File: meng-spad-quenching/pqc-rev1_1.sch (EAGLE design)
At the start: 54 parts, among them IC1 ADCMP582, IC3 LT3032-5, J1 VIN_LOGIC, U1 SN65EPT21DGK, U2 TPS78233DDCT, U3 SN65EPT22DGK, X1 CONN_SPAD, X2 CONN_SCOPE_COMP, X3 CONN_SCOPE_RSHUNT, X4 CONN_VA_BIAS, X5 CONN_LATCH_IN

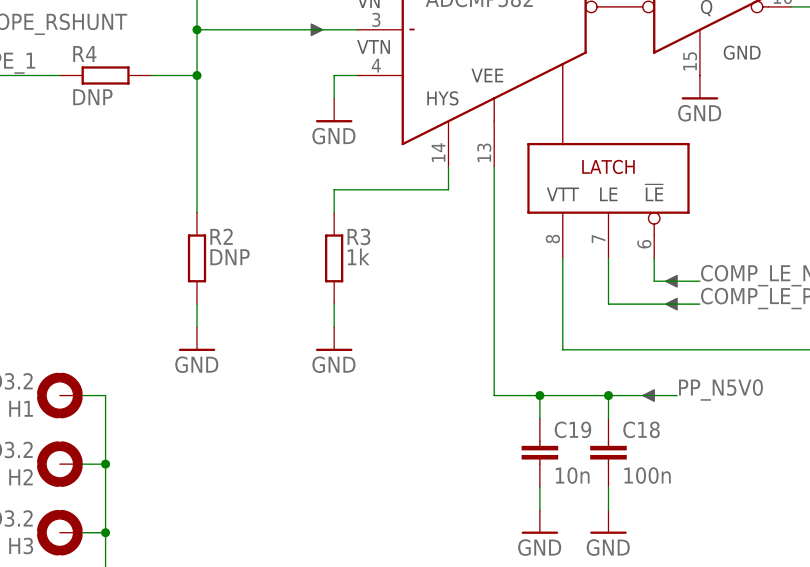
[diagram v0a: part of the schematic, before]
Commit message: Moved to PQC rev. 1.1 --- fixed hysteresis resistor connection.
Hysteresis resistor (R3) should be connected to comparator negative
supply rail, not GND. Re-exported Gerbers.
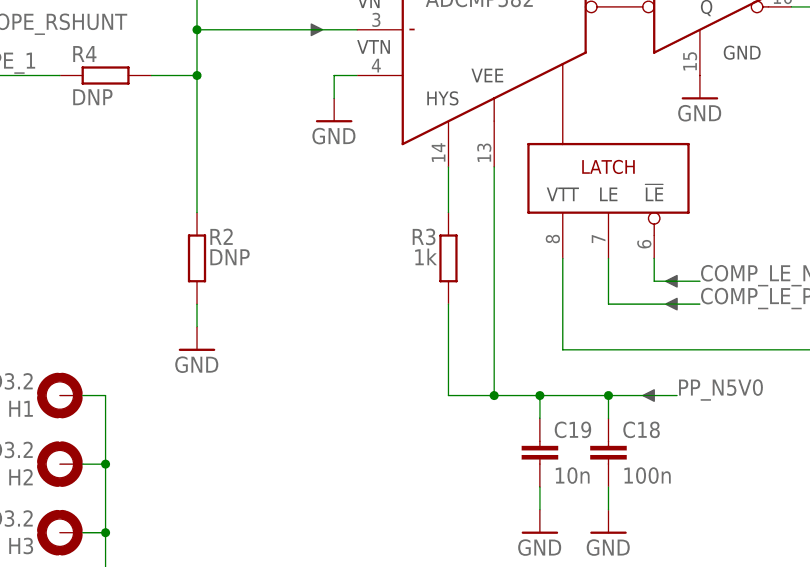
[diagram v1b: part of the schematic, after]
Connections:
- net GND: no longer R3.1
- net PP_N5V0: now also R3.1
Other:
- moved on the sheet: R3
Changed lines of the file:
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@@
 <grid distance="0.1" unitdist="inch" unit="inch" style="lines" multiple="1" display="yes" altdistance="0.01" altunitdist="inch" altunit="inch"/>
 <layers>
-<layer number="1" name="Top" color="4" fill="1" visible="yes" active="no"/>
-<layer number="2" name="Route2" color="3" fill="1" visible="yes" active="no"/>
-<layer number="3" name="Route3" color="4" fill="3" visible="yes" active="no"/>
-<layer number="4" name="Route4" color="1" fill="4" visible="yes" active="no"/>
-<layer number="5" name="Route5" color="4" fill="4" visible="yes" active="no"/>
-<layer number="6" name="Route6" color="1" fill="8" visible="yes" active="no"/>
-<layer number="7" name="Route7" color="4" fill="8" visible="yes" active="no"/>
-<layer number="8" name="Route8" color="1" fill="2" visible="yes" active="no"/>
-<layer number="9" name="Route9" color="4" fill="2" visible="yes" active="no"/>
-<layer number="10" name="Route10" color="1" fill="7" visible="yes" active="no"/>
-<layer number="11" name="Route11" color="4" fill="7" visible="yes" active="no"/>
-<layer number="12" name="Route12" color="1" fill="5" visible="yes" active="no"/>
-<layer number="13" name="Route13" color="4" fill="5" visible="yes" active="no"/>
-<layer number="14" name="Route14" color="1" fill="6" visible="yes" active="no"/>
-<layer number="15" name="Route15" color="6" fill="1" visible="yes" active="no"/>
-<layer number="16" name="Bottom" color="1" fill="1" visible="yes" active="no"/>
-<layer number="17" name="Pads" color="2" fill="1" visible="yes" active="no"/>
-<layer number="18" name="Vias" color="2" fill="1" visible="yes" active="no"/>
-<layer number="19" name="Unrouted" color="6" fill="1" visible="yes" active="no"/>
-<layer number="20" name="Dimension" color="15" fill="1" visible="yes" active="no"/>
-<layer number="21" name="tPlace" color="7" fill="1" visible="yes" active="no"/>
-<layer number="22" name="bPlace" color="7" fill="1" visible="yes" active="no"/>
-<layer number="23" name="tOrigins" color="15" fill="1" visible="yes" active="no"/>
-<layer number="24" name="bOrigins" color="15" fill="1" visible="yes" active="no"/>
-<layer number="25" name="tNames" color="7" fill="1" visible="yes" active="no"/>
-<layer number="26" name="bNames" color="7" fill="1" visible="yes" active="no"/>
-<layer number="27" name="tValues" color="7" fill="1" visible="yes" active="no"/>
-<layer number="28" name="bValues" color="7" fill="1" visible="yes" active="no"/>
+<layer number="1" name="Top" color="4" fill="1" visible="no" active="no"/>
+<layer number="2" name="Route2" color="3" fill="1" visible="no" active="no"/>
+<layer number="3" name="Route3" color="4" fill="3" visible="no" active="no"/>
+<layer number="4" name="Route4" color="1" fill="4" visible="no" active="no"/>
+<layer number="5" name="Route5" color="4" fill="4" visible="no" active="no"/>
+<layer number="6" name="Route6" color="1" fill="8" visible="no" active="no"/>
+<layer number="7" name="Route7" color="4" fill="8" visible="no" active="no"/>
+<layer number="8" name="Route8" color="1" fill="2" visible="no" active="no"/>
+<layer number="9" name="Route9" color="4" fill="2" visible="no" active="no"/>
+<layer number="10" name="Route10" color="1" fill="7" visible="no" active="no"/>
+<layer number="11" name="Route11" color="4" fill="7" visible="no" active="no"/>
+<layer number="12" name="Route12" color="1" fill="5" visible="no" active="no"/>
+<layer number="13" name="Route13" color="4" fill="5" visible="no" active="no"/>
+<layer number="14" name="Route14" color="1" fill="6" visible="no" active="no"/>
+<layer number="15" name="Route15" color="6" fill="1" visible="no" active="no"/>
+<layer number="16" name="Bottom" color="1" fill="1" visible="no" active="no"/>
+<layer number="17" name="Pads" color="2" fill="1" visible="no" active="no"/>
+<layer number="18" name="Vias" color="2" fill="1" visible="no" active="no"/>
+<layer number="19" name="Unrouted" color="6" fill="1" visible="no" active="no"/>
+<layer number="20" name="Dimension" color="15" fill="1" visible="no" active="no"/>
+<layer number="21" name="tPlace" color="7" fill="1" visible="no" active="no"/>
+<layer number="22" name="bPlace" color="7" fill="1" visible="no" active="no"/>
+<layer number="23" name="tOrigins" color="15" fill="1" visible="no" active="no"/>
+<layer number="24" name="bOrigins" color="15" fill="1" visible="no" active="no"/>
+<layer number="25" name="tNames" color="7" fill="1" visible="no" active="no"/>
+<layer number="26" name="bNames" color="7" fill="1" visible="no" active="no"/>
+<layer number="27" name="tValues" color="7" fill="1" visible="no" active="no"/>
+<layer number="28" name="bValues" color="7" fill="1" visible="no" active="no"/>
 <layer number="29" name="tStop" color="7" fill="3" visible="no" active="no"/>
 <layer number="30" name="bStop" color="7" fill="6" visible="no" active="no"/>
@@
 <layer number="35" name="tGlue" color="7" fill="4" visible="no" active="no"/>
 <layer number="36" name="bGlue" color="7" fill="5" visible="no" active="no"/>
-<layer number="37" name="tTest" color="7" fill="1" visible="yes" active="no"/>
-<layer number="38" name="bTest" color="7" fill="1" visible="yes" active="no"/>
+<layer number="37" name="tTest" color="7" fill="1" visible="no" active="no"/>
+<layer number="38" name="bTest" color="7" fill="1" visible="no" active="no"/>
 <layer number="39" name="tKeepout" color="4" fill="11" visible="no" active="no"/>
 <layer number="40" name="bKeepout" color="1" fill="11" visible="no" active="no"/>
@@
 <layer number="44" name="Drills" color="7" fill="1" visible="no" active="no"/>
 <layer number="45" name="Holes" color="7" fill="1" visible="no" active="no"/>
-<layer number="46" name="Milling" color="3" fill="1" visible="yes" active="no"/>
-<layer number="47" name="Measures" color="7" fill="1" visible="yes" active="no"/>
-<layer number="48" name="Document" color="7" fill="1" visible="yes" active="no"/>
-<layer number="49" name="Reference" color="7" fill="1" visible="yes" active="no"/>
-<layer number="50" name="dxf" color="7" fill="1" visible="yes" active="no"/>
-<layer number="51" name="tDocu" color="7" fill="1" visible="yes" active="no"/>
-<layer number="52" name="bDocu" color="7" fill="1" visible="yes" active="no"/>
-<layer number="53" name="tPadExt" color="7" fill="1" visible="yes" active="no"/>
-<layer number="54" name="bPadExt" color="1" fill="1" visible="yes" active="no"/>
-<layer number="56" name="wert" color="7" fill="1" visible="yes" active="no"/>
+<layer number="46" name="Milling" color="3" fill="1" visible="no" active="no"/>
+<layer number="47" name="Measures" color="7" fill="1" visible="no" active="no"/>
+<layer number="48" name="Document" color="7" fill="1" visible="no" active="no"/>
+<layer number="49" name="Reference" color="7" fill="1" visible="no" active="no"/>
+<layer number="50" name="dxf" color="7" fill="1" visible="no" active="no"/>
+<layer number="51" name="tDocu" color="7" fill="1" visible="no" active="no"/>
+<layer number="52" name="bDocu" color="7" fill="1" visible="no" active="no"/>
+<layer number="53" name="tPadExt" color="7" fill="1" visible="no" active="no"/>
+<layer number="54" name="bPadExt" color="1" fill="1" visible="no" active="no"/>
+<layer number="56" name="wert" color="7" fill="1" visible="no" active="no"/>
 <layer number="90" name="Modules" color="5" fill="1" visible="no" active="no"/>
 <layer number="91" name="Nets" color="2" fill="1" visible="yes" active="yes"/>
@@
 <part name="GND3" library="supply1" deviceset="GND" device=""/>
 <part name="R3" library="rcl" deviceset="R-EU_" device="R0805" value="1k"/>
-<part name="GND4" library="supply1" deviceset="GND" device=""/>
 <part name="X1" library="con-coax" deviceset="SMA-" device="142-0711-871/876" value="CONN_SPAD"/>
 <part name="X2" library="con-coax" deviceset="SMA-" device="142-0711-871/876" value="CONN_SCOPE_COMP"/>
@@
 <attribute name="VALUE" x="53.34" y="93.98" size="1.778" layer="96"/>
 </instance>
-<instance part="R3" gate="G$1" x="71.12" y="106.68" smashed="yes" rot="R90">
-<attribute name="NAME" x="72.39" y="108.1786" size="1.778" layer="95"/>
-<attribute name="VALUE" x="72.39" y="105.918" size="1.778" layer="96"/>
-</instance>
-<instance part="GND4" gate="1" x="71.12" y="96.52" smashed="yes">
-<attribute name="VALUE" x="68.58" y="93.98" size="1.778" layer="96"/>
+<instance part="R3" gate="G$1" x="83.82" y="106.68" smashed="yes" rot="MR90">
+<attribute name="NAME" x="82.55" y="108.1786" size="1.778" layer="95" rot="MR0"/>
+<attribute name="VALUE" x="82.55" y="105.918" size="1.778" layer="96" rot="MR0"/>
 </instance>
 <instance part="X1" gate="G1" x="25.4" y="167.64" smashed="yes">
@@
 <pinref part="R2" gate="G$1" pin="1"/>
 <wire x1="55.88" y1="99.06" x2="55.88" y2="101.6" width="0.1524" layer="91"/>
-</segment>
-<segment>
-<pinref part="GND4" gate="1" pin="GND"/>
-<pinref part="R3" gate="G$1" pin="1"/>
-<wire x1="71.12" y1="99.06" x2="71.12" y2="101.6" width="0.1524" layer="91"/>
 </segment>
 <segment>
@@
 <segment>
 <pinref part="IC1" gate="G$1" pin="HYS"/>
-<wire x1="83.82" y1="116.84" x2="83.82" y2="114.3" width="0.1524" layer="91"/>
-<wire x1="83.82" y1="114.3" x2="71.12" y2="114.3" width="0.1524" layer="91"/>
 <pinref part="R3" gate="G$1" pin="2"/>
-<wire x1="71.12" y1="114.3" x2="71.12" y2="111.76" width="0.1524" layer="91"/>
+<wire x1="83.82" y1="116.84" x2="83.82" y2="111.76" width="0.1524" layer="91"/>
 </segment>
 </net>
@@
 <junction x="93.98" y="91.44"/>
 <junction x="101.6" y="91.44"/>
-</segment>
-<segment>
+<pinref part="R3" gate="G$1" pin="1"/>
+<wire x1="88.9" y1="91.44" x2="83.82" y2="91.44" width="0.1524" layer="91"/>
+<wire x1="83.82" y1="91.44" x2="83.82" y2="101.6" width="0.1524" layer="91"/>
+<junction x="88.9" y="91.44"/>
+</segment>
+<segment>

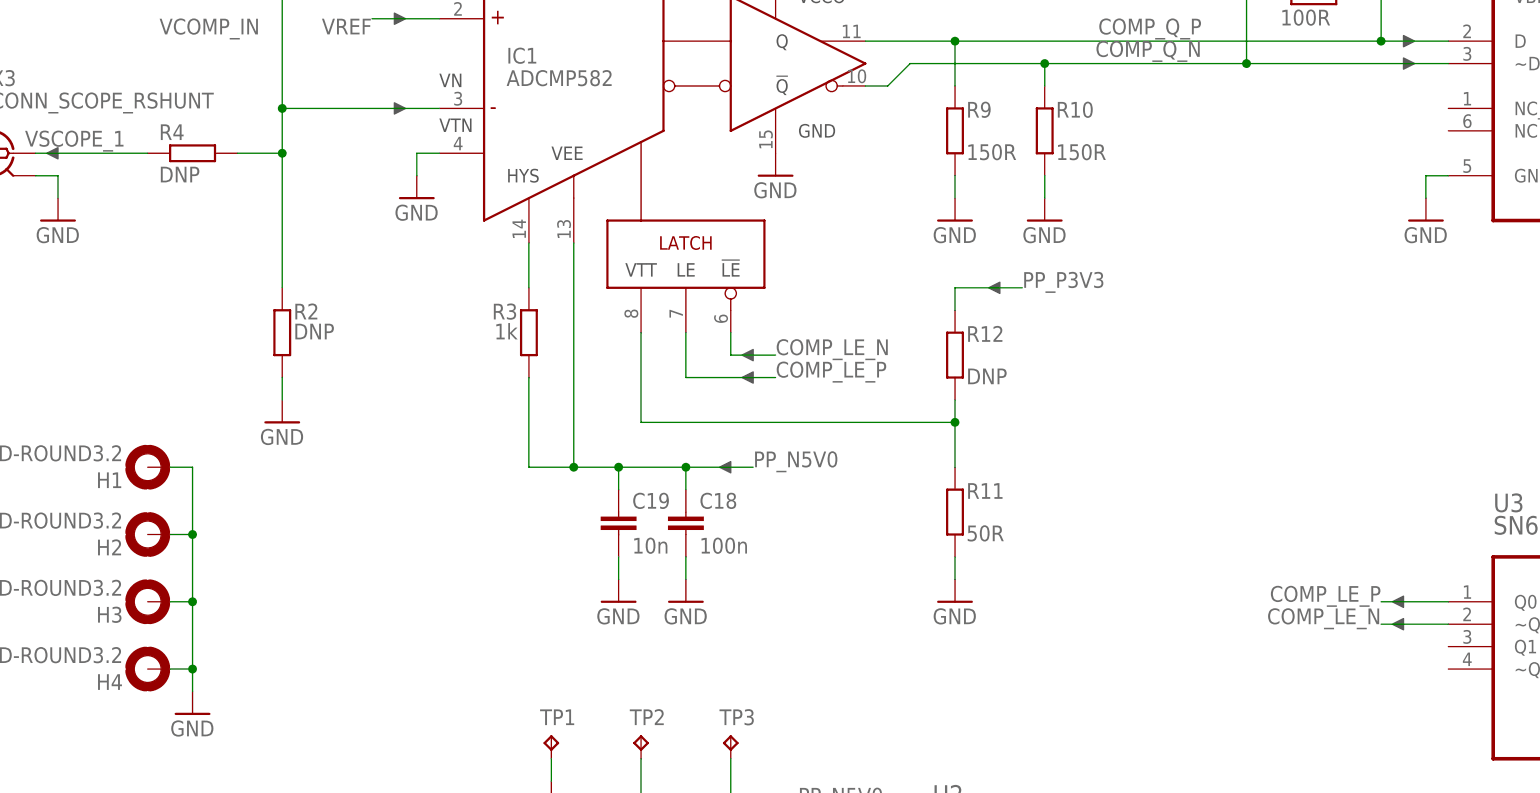
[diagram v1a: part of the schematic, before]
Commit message: Fixed some lingering bugs
Removed T-termination pullup (not necessary). Flipped LATCH polarity so
SMA is active-high and can be left floating.
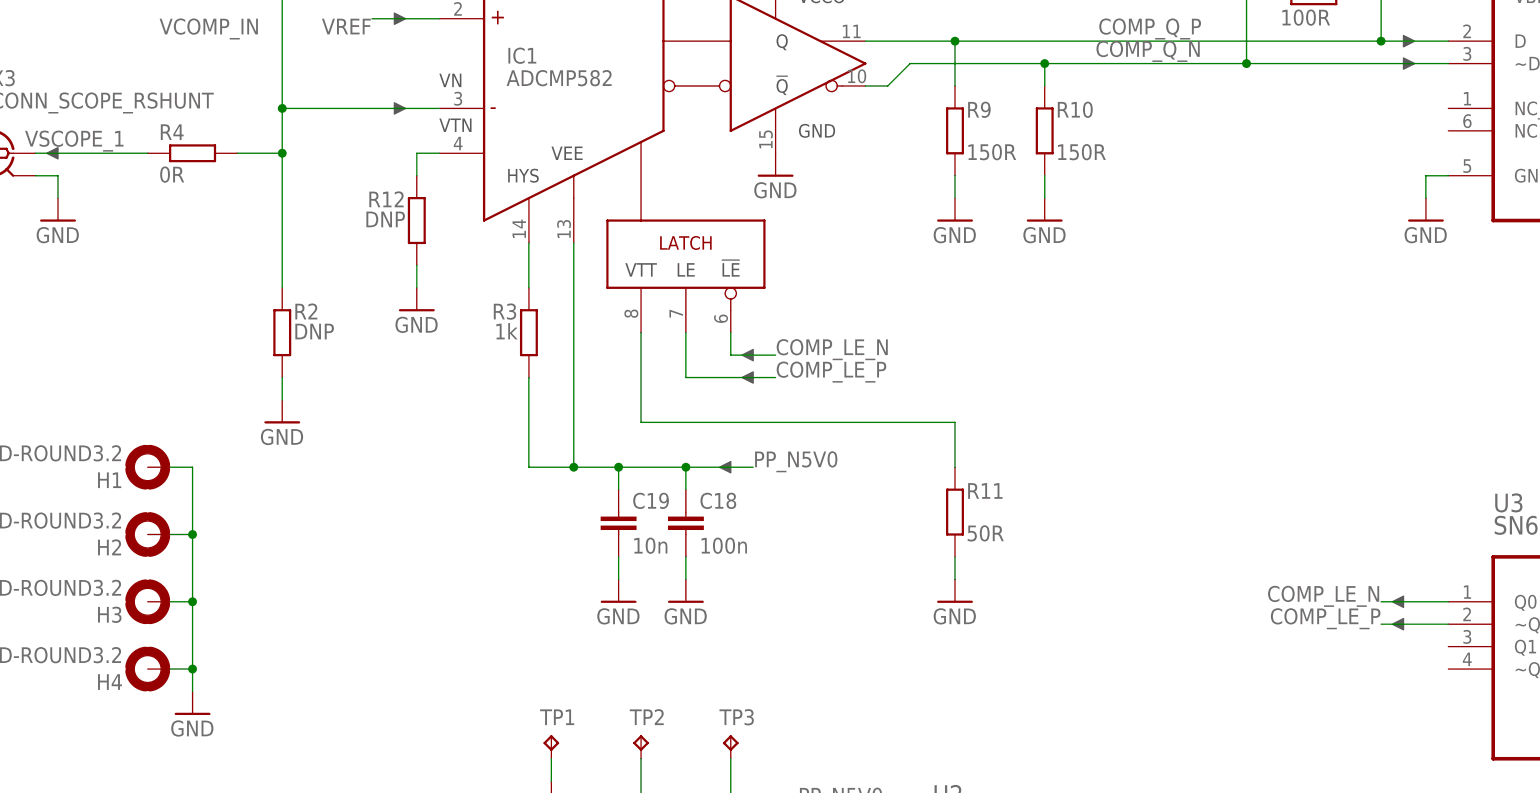
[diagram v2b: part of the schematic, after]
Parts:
- R4: value DNP -> 0R
- R6: device rcl:R-EU_R0805 -> rcl:R-EU_R0603
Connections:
- new net N$3: IC1.VTN, R12.2
- net COMP_LE_N: now also U3.Q0; no longer U3.~Q0
- net COMP_LE_P: now also U3.~Q0; no longer U3.Q0
- net GND: now also R12.1; no longer IC1.VTN
- net N$6: no longer R12.2
- net PP_P3V3: no longer R12.1
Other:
- note added: "Default behavior is now non-latching"
- note added: "Latch SMA is now active-high"
- note added: "Note: flipped this diffpair from rev. 1"
- note added: "Other 2 resistors are inside the comparator"
- moved on the sheet: R12
